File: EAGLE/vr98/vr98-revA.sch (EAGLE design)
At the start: 454 parts, among them Q1 2N7002, Q2 DMG2305UX-7, Q3 IRLML6401, Q4 2N2222, U1 STM32F411CEU7, U2 74HC589A_DT, U3 74HC589A_DT, U4 74HC589A_DT, U5 M25C, Y1 32.768kHz ±20ppm 6pF, Y2 25MHz 9pF

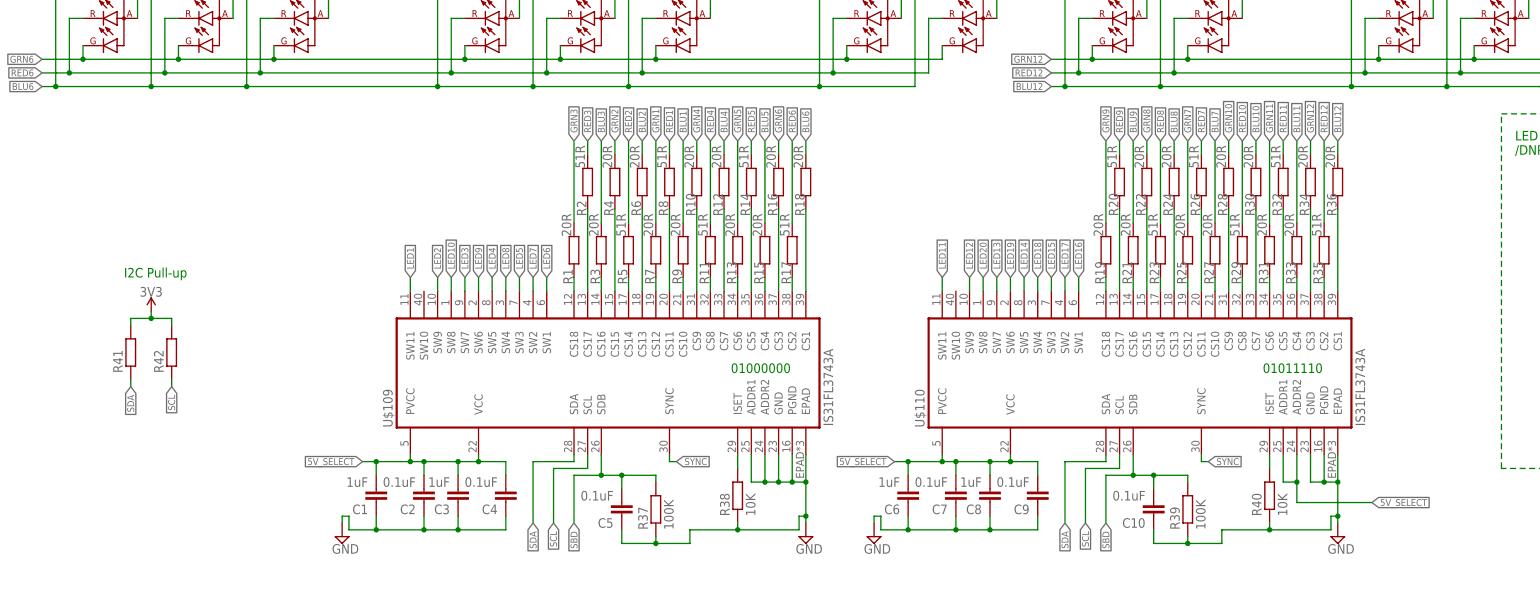
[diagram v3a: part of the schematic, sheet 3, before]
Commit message: move to ISP LED driver
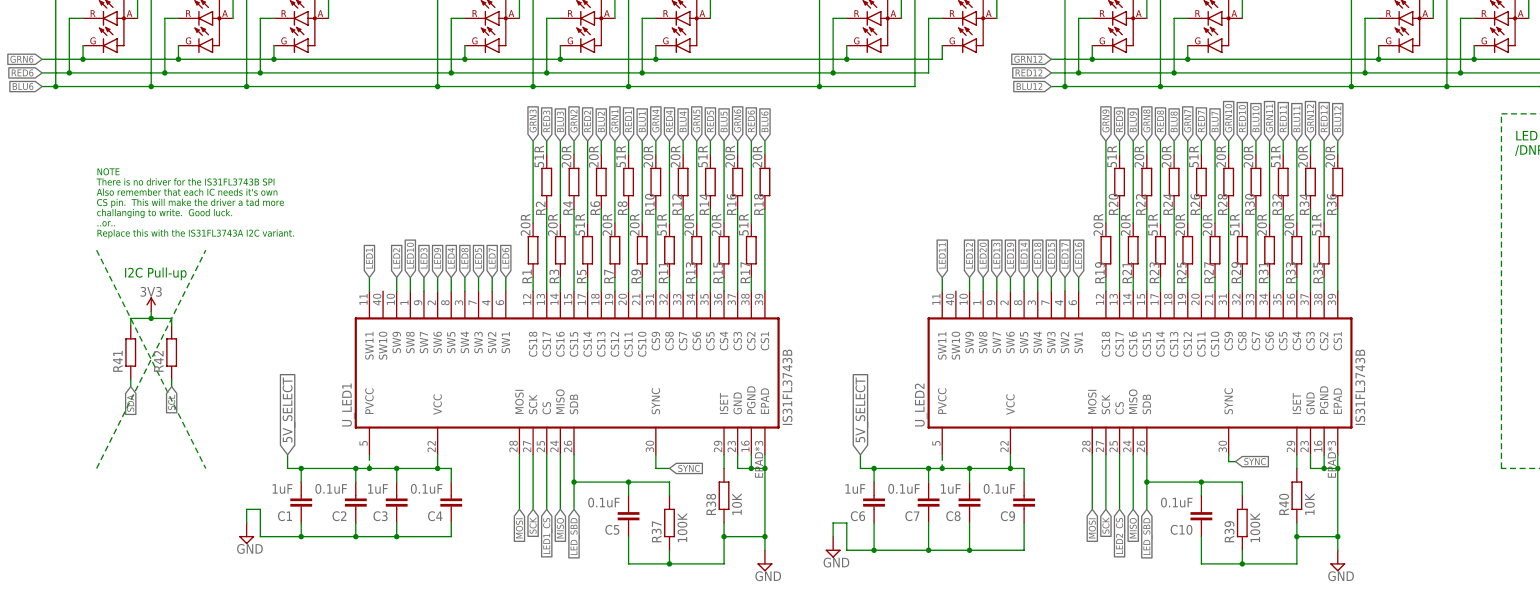
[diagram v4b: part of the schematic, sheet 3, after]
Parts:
- removed U$109, U$110: IS31FL3743A, __untitled:IS31FL3743A
- added U_LED1, U_LED2: IS31FL3743B, ts_kb_mcu:IS31FL3743B
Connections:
- removed net N$137: R40.2, U$110.ISET
- removed net RX: U1A.PA10
- removed net SBD: C10.2, C5.2, R37.2, R39.2, U$109.SDB, U$110.SDB
- removed net TX: U1A.PA9
- new net LED1_CS: U1A.PA9, U_LED1.CS
- new net LED2_CS: U1A.PA10, U_LED2.CS
- new net LED_SBD: C10.2, C5.2, R37.2, R39.2, U_LED1.SDB, U_LED2.SDB
- new net LED_SDB: U1A.PB5
- new net N$151: R40.2, U_LED2.ISET
- net 5V_SELECT: now also U_LED1.PVCC, U_LED1.VCC, U_LED2.PVCC, U_LED2.VCC; no longer U$109.PVCC, U$109.VCC, U$110.ADDR1, U$110.ADDR2, U$110.PVCC, U$110.VCC
- net GND: now also U_LED1.EPAD, U_LED1.GND, U_LED1.PGND, U_LED2.EPAD, U_LED2.GND, U_LED2.PGND; no longer U$109.ADDR1, U$109.ADDR2, U$109.EPAD, U$109.GND, U$109.PGND, U$110.EPAD, U$110.GND, U$110.PGND
- net LED1: now also U_LED1.SW11; no longer U$109.SW11
- net LED10: now also U_LED1.SW8; no longer U$109.SW8
- net LED11: now also U_LED2.SW11; no longer U$110.SW11
- net LED12: now also U_LED2.SW9; no longer U$110.SW9
- net LED13: now also U_LED2.SW7; no longer U$110.SW7
- net LED14: now also U_LED2.SW5; no longer U$110.SW5
- net LED15: now also U_LED2.SW3; no longer U$110.SW3
- net LED16: now also U_LED2.SW1; no longer U$110.SW1
- net LED17: now also U_LED2.SW2; no longer U$110.SW2
- net LED18: now also U_LED2.SW4; no longer U$110.SW4
- net LED19: now also U_LED2.SW6; no longer U$110.SW6
- net LED2: now also U_LED1.SW9; no longer U$109.SW9
- net LED20: now also U_LED2.SW8; no longer U$110.SW8
- net LED3: now also U_LED1.SW7; no longer U$109.SW7
- net LED4: now also U_LED1.SW5; no longer U$109.SW5
- net LED5: now also U_LED1.SW3; no longer U$109.SW3
- net LED6: now also U_LED1.SW1; no longer U$109.SW1
- net LED7: now also U_LED1.SW2; no longer U$109.SW2
- net LED8: now also U_LED1.SW4; no longer U$109.SW4
- net LED9: now also U_LED1.SW6; no longer U$109.SW6
- net MISO: now also U_LED1.MISO, U_LED2.MISO
- net MOSI: now also U_LED1.MOSI, U_LED2.MOSI
- net N$10: now also U_LED2.CS8; no longer U$110.CS8
- net N$11: now also U_LED2.CS9; no longer U$110.CS9
- net N$12: now also U_LED2.CS10; no longer U$110.CS10
- net N$123: now also U_LED1.CS5; no longer U$109.CS5
- net N$124: now also U_LED1.CS6; no longer U$109.CS6
- net N$125: now also U_LED1.CS7; no longer U$109.CS7
- net N$126: now also U_LED1.CS8; no longer U$109.CS8
- net N$127: now also U_LED1.CS9; no longer U$109.CS9
- net N$128: now also U_LED1.CS10; no longer U$109.CS10
- net N$129: now also U_LED1.CS11; no longer U$109.CS11
- net N$13: now also U_LED2.CS11; no longer U$110.CS11
- net N$130: now also U_LED1.CS12; no longer U$109.CS12
- net N$131: now also U_LED1.CS14; no longer U$109.CS14
- net N$132: now also U_LED1.CS15; no longer U$109.CS15
- net N$133: now also U_LED1.CS16; no longer U$109.CS16
- net N$134: now also U_LED1.CS17; no longer U$109.CS17
- net N$135: now also U_LED1.CS18; no longer U$109.CS18
- net N$136: now also U_LED1.ISET; no longer U$109.ISET
- net N$14: now also U_LED2.CS12; no longer U$110.CS12
- net N$15: now also U_LED2.CS14; no longer U$110.CS14
- net N$153: now also U_LED1.CS13; no longer U$109.CS13
- net N$16: now also U_LED2.CS15; no longer U$110.CS15
- net N$17: now also U_LED2.CS16; no longer U$110.CS16
- net N$18: now also U_LED2.CS17; no longer U$110.CS17
- net N$19: now also U_LED2.CS18; no longer U$110.CS18
- net N$20: now also U_LED2.CS13; no longer U$110.CS13
- net N$21: now also U_LED1.CS1; no longer U$109.CS1
- net N$22: now also U_LED1.CS2; no longer U$109.CS2
- net N$23: now also U_LED1.CS3; no longer U$109.CS3
- net N$24: now also U_LED1.CS4; no longer U$109.CS4
- net N$3: now also U_LED2.CS1; no longer U$110.CS1
- net N$4: now also U_LED2.CS2; no longer U$110.CS2
- net N$5: now also U_LED2.CS3; no longer U$110.CS3
- net N$6: now also U_LED2.CS4; no longer U$110.CS4
- net N$7: now also U_LED2.CS5; no longer U$110.CS5
- net N$8: now also U_LED2.CS6; no longer U$110.CS6
- net N$9: now also U_LED2.CS7; no longer U$110.CS7
- net SCK: now also U_LED1.SCK, U_LED2.SCK
- net SCL: no longer U$109.SCL, U$110.SCL
- net SDA: no longer U$109.SDA, U$110.SDA
- net SYNC: now also U_LED1.SYNC, U_LED2.SYNC; no longer U$109.SYNC, U$110.SYNC
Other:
- note added: "NOTE There is no driver for the IS31FL3743B SPI Also remember that each IC needs it's own CS pin. This will make the driver a tad more challanging to write. Good luck. ..or.. Replace this with the IS31FL3743A I2C variant."
- note removed: "01000000"
- note removed: "01011110"
- moved on the sheet: C1, C10, C2, C28, C3, C4, C5, C6, C7, C8, C9, R1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

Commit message: updates
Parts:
- removed D100, D103, D104: (no value), jlcpcb_basic_parts:1N5819WS
- removed J2: (no value), ts_keyboards:UBD-S1_C4
- removed R1, R10, R12, R13, R15, R16, R18, R19, R21, R22, R24, R25, R27, R28, R3, R30, R31, R33, R34, R36, R4, R6, R7, R9: 20R, rcl:R-EU_R0603
- removed R11, R14, R17, R2, R20, R23, R26, R29, R32, R35, R5, R8: 51R, rcl:R-EU_R0603
- removed R47, R48, R49, R50, R51, R52, R53, R54, R55, R56, R57, R58, R59, R60, R61, R62, R63, R64: 10K, rcl:R-EU_R0603
- removed S2: KEY, SparkFun-Switches:MOMENTARY-SWITCH-SPST-SMD-5.2-TALL-REDUNDANT
- removed SW_CL_2, SW_SPC_2, SW_SPC_3: MX-5-PIN-MILMAX-3305-XNO-SILK, ts_keyboards:MX-5-PIN-MILMAX-3305-XNO-SILK
- removed SW_DP_2, SW_ENT_2, SW_F13_2, SW_LS_2, SW_NUBS: MX-5-PIN-HOTSWAP-PADNO-SILK, ts_keyboards:MX-5-PIN-HOTSWAP-PADNO-SILK
- removed SW_FN: MX-5-PIN-HOTSWAP-PAD, ts_keyboards:MX-5-PIN-HOTSWAP-PAD
- removed U$100, U$32, U$38, U$58, U$75, U$83, U$99: 156120M173000, ts_keyboards:156120M173000
- removed U$108: DNP, ts_keyboards:156120M173000
- added H_BSP, H_ENT, H_LS, H_NEN, H_NP, H_RS: MX-STABS-200U, ts_keyboards:MX-STABS-200U
- added H_SPC: MX-STABS-625U, ts_keyboards:MX-STABS-625U
- added RA1, RA2, RA3, RA4, RA5: 10K, __untitled:R-EU-4_
- added RA10, RA13, RA14, RA15, RA8, RA9: 20R, __untitled:R-EU-4_
- added RA11, RA12, RA6, RA7: 51R, __untitled:R-EU-4_
- added UDB1: (no value), ts_keyboards:UBD-S1_C4
- added UDB2: (no value), ts_keyboards:UBD-C3
- added Z1, Z10, Z101, Z103, Z104, Z107, Z11, Z12, Z13, Z14, Z15, Z16, Z17, Z2, Z20, Z21, Z22, Z23, Z24, Z25, Z26, Z27, Z28, Z3, Z4, Z6, Z7, Z8, Z9, Z94: 156120M173000, ts_keyboards:156120M173000
- added Z19: DNP, ts_keyboards:156120M173000
- D101: value (none) -> DNP
- J1: device ts_keyboards:UBD-C3 -> SparkFun-Connectors:CONN_02
- JKEY: value (none) -> MOLEX_0781710005; device __untitled:MOLEX_0781710004 -> molex-pico-ezmate:MOLEX_0781710005
- SW_F17: device untitled:EC11E15244B2 -> ts_keyboards:EC11E15244B2
- U$1, U$10, U$11, U$12, U$13, U$14, U$15, U$16, U$17, U$18, U$19, U$2, U$20, U$21, U$22, U$23, U$24, U$25, U$26, U$27, U$6, U$7, U$8, U$9: value 156120M173000 -> TEST_PAD; device ts_keyboards:156120M173000 -> ts_keyboards:TEST_PAD
- U$3, U$4: value 156120M173000 -> MOLEX_0781710006; device ts_keyboards:156120M173000 -> molex-pico-ezmate:MOLEX_0781710006
- renumbered U$101 to Z92, U$102 to Z93, U$103 to Z95, U$104 to Z96, U$105 to Z97, U$106 to Z98, U$107 to Z99, U$28 to Z29, U$29 to Z30, U$30 to Z31, U$31 to Z32, U$33 to Z33, U$34 to Z34, U$35 to Z35, U$36 to Z36, U$37 to Z37, U$39 to Z38, U$40 to Z39, U$41 to Z40, U$42 to Z41, U$43 to Z42, U$44 to Z43, U$45 to Z44, U$46 to Z45, U$47 to Z46, U$48 to Z47, U$49 to Z48, U$5 to Z5, U$50 to Z49, U$51 to Z50, U$52 to Z102, U$53 to Z51, U$54 to Z52, U$55 to Z53, U$56 to Z54, U$57 to Z55, U$59 to Z56, U$60 to Z57, U$61 to Z58, U$62 to Z59, U$63 to Z60, U$64 to Z61, U$65 to Z62, U$66 to Z63, U$67 to Z64, U$68 to Z65, U$69 to Z66, U$70 to Z67, U$71 to Z68, U$72 to Z69, U$73 to Z70, U$74 to Z71, U$76 to Z72, U$77 to Z73, U$78 to Z74, U$79 to Z75, U$80 to Z76, U$81 to Z77, U$82 to Z78, U$84 to Z79, U$85 to Z80, U$86 to Z81, U$87 to Z82, U$88 to Z83, U$89 to Z84, U$90 to Z85, U$91 to Z86, U$92 to Z87, U$93 to Z88, U$94 to Z89, U$95 to Z90, U$96 to Z105, U$97 to Z91, U$98 to Z106
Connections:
- net LED_EN renamed LED_PWR_EN
- removed net K_F13: D18.A, SW_F13_2.S, SW_F17.D
- new net N$152: SW_F17.A, U$4.5
- new net N$156: D102.A, JKEY.5
- new net N$157: D18.A, U$3.4
- net BLU1: now also RA9B.1, Z1.B, Z2.B, Z3.B, Z4.B, Z6.B, Z7.B, Z8.B, Z9.B; no longer R9.2, U$1.B, U$2.B, U$3.B, U$4.B, U$6.B, U$7.B, U$8.B, U$9.B
- net BLU10: now also RA14D.2, Z103.B; no longer R30.2
- net BLU11: now also RA15B.1; no longer R33.2
- net BLU12: now also RA15D.2, Z94.B; no longer R36.2
- net BLU2: now also RA8D.2, Z19.B, Z20.B, Z21.B, Z22.B, Z23.B, Z24.B, Z25.B, Z26.B, Z27.B, Z28.B; no longer R6.2, U$18.B, U$19.B, U$20.B, U$21.B, U$22.B, U$23.B, U$24.B, U$25.B, U$26.B, U$27.B
- net BLU3: now also RA8B.1; no longer R3.2, U$38.B
- net BLU4: now also RA9D.2; no longer R12.2, U$58.B
- net BLU5: now also RA10B.1; no longer R15.2, U$75.B, U$83.B
- net BLU6: now also RA10D.2, Z104.B, Z107.B; no longer R18.2, U$100.B, U$99.B
- net BLU7: now also RA14B.1, Z10.B, Z11.B, Z12.B, Z13.B, Z14.B, Z15.B, Z16.B, Z17.B; no longer R27.2, U$10.B, U$108.B, U$11.B, U$12.B, U$13.B, U$14.B, U$15.B, U$16.B, U$17.B
- net BLU8: now also RA13D.2, Z101.B; no longer R24.2, U$32.B
- net BLU9: now also RA13B.1; no longer R21.2
- net COL0: now also RA1A.2, U$11.P$1; no longer R47.2
- net COL1: now also RA1B.1, U$12.P$1; no longer R48.2
- net COL10: now also D94.C, RA3C.1, U$21.P$1; no longer D95.C, R57.2
- net COL11: now also RA3D.2, U$22.P$1; no longer R58.2
- net COL12: now also D95.C, RA4A.2, U$23.P$1; no longer D96.C, R59.2
- net COL13: now also D96.C, RA4B.1, U$24.P$1; no longer D97.C, R60.2, SW_DP_2.P, SW_ENT_2.P
- net COL14: now also D97.C, RA4C.1, U$25.P$1; no longer D98.C, R61.2
- net COL15: now also D98.C, RA4D.2, U$26.P$1; no longer D99.C, R62.2
- net COL16: now also D99.C, RA5A.2, U$27.P$1; no longer D100.C, R63.2
- net COL17: now also RA5B.1, U$1.P$1; no longer R64.2, SW_F13_2.P
- net COL2: now also RA1C.1, U$13.P$1; no longer D101.C, R49.2
- net COL3: now also RA1D.2, U$14.P$1; no longer D103.C, R50.2
- net COL4: now also D101.C, RA2A.2, U$15.P$1; no longer D102.C, R51.2
- net COL5: now also RA2B.1, U$16.P$1; no longer R52.2
- net COL6: now also D102.C, RA2C.1, U$17.P$1; no longer D104.C, R53.2
- net COL7: now also RA2D.2, U$18.P$1; no longer D92.C, R54.2
- net COL8: now also D92.C, RA3A.2, U$19.P$1; no longer D93.C, R55.2
- net COL9: now also D93.C, RA3B.1, U$20.P$1; no longer D94.C, R56.2
- net ENC_A: now also R43.1, U$3.6; no longer R44.1, SW_F17.A
- net ENC_B: now also R44.1, U$3.5; no longer R43.1, SW_F17.B
- net GND: now also J1.1, JKEY.1, JKEY.M, SW_F17.GND, U$3.1, U$3.M, U$4.1, U$4.M, UDB1.GND, UDB1.M, UDB2.GND, UDB2.M; no longer J1.GND, J2.GND, JKEY.4, SW_F17.1, SW_F17.2, SW_F17.C
- net GND2: now also RA1A.1, RA1B.2, RA1C.2, RA1D.1, RA2A.1, RA2B.2, RA2C.2, RA2D.1, RA3A.1, RA3B.2, RA3C.2, RA3D.1, RA4A.1, RA4B.2, RA4C.2, RA4D.1, RA5A.1, RA5B.2; no longer R47.1, R48.1, R49.1, R50.1, R51.1, R52.1, R53.1, R54.1, R55.1, R56.1, R57.1, R58.1, R59.1, R60.1, R61.1, R62.1, R63.1, R64.1
- net GRN1: now also RA9A.2, Z1.G, Z2.G, Z3.G, Z4.G, Z6.G, Z7.G, Z8.G, Z9.G; no longer R7.2, U$1.G, U$2.G, U$3.G, U$4.G, U$6.G, U$7.G, U$8.G, U$9.G
- net GRN10: now also RA14C.1, Z103.G; no longer R28.2
- net GRN11: now also RA15A.2; no longer R31.2
- net GRN12: now also RA15C.1, Z94.G; no longer R34.2
- net GRN2: now also RA8C.1, Z19.G, Z20.G, Z21.G, Z22.G, Z23.G, Z24.G, Z25.G, Z26.G, Z27.G, Z28.G; no longer R4.2, U$18.G, U$19.G, U$20.G, U$21.G, U$22.G, U$23.G, U$24.G, U$25.G, U$26.G, U$27.G
- net GRN3: now also RA8A.2; no longer R1.2, U$38.G
- net GRN4: now also RA9C.1; no longer R10.2, U$58.G
- net GRN5: now also RA10A.2; no longer R13.2, U$75.G, U$83.G
- net GRN6: now also RA10C.1, Z104.G, Z107.G; no longer R16.2, U$100.G, U$99.G
- net GRN7: now also RA14A.2, Z10.G, Z11.G, Z12.G, Z13.G, Z14.G, Z15.G, Z16.G, Z17.G; no longer R25.2, U$10.G, U$108.G, U$11.G, U$12.G, U$13.G, U$14.G, U$15.G, U$16.G, U$17.G
- net GRN8: now also RA13C.1, Z101.G; no longer R22.2, U$32.G
- net GRN9: now also RA13A.2; no longer R19.2
- net K_CL: no longer SW_CL_2.P
- net K_DP: no longer SW_DP_2.S
- net K_ENT: no longer SW_ENT_2.S
- net K_LS: no longer SW_LS_2.P
- net LED1: now also Z1.A, Z19.A; no longer U$1.A, U$18.A
- net LED10: now also Z28.A, Z9.A; no longer U$100.A, U$27.A, U$83.A, U$9.A
- net LED11: now also Z10.A; no longer U$10.A
- net LED12: now also Z11.A; no longer U$11.A
- net LED13: now also Z12.A, Z94.A; no longer U$12.A
- net LED14: now also Z13.A; no longer U$13.A
- net LED15: no longer U$32.A
- net LED16: now also Z101.A, Z103.A, Z14.A; no longer U$14.A
- net LED17: now also Z15.A; no longer U$15.A
- net LED18: now also Z16.A; no longer U$16.A
- net LED19: now also Z17.A; no longer U$17.A
- net LED2: now also Z20.A; no longer U$19.A, U$38.A, U$58.A, U$75.A
- net LED20: no longer U$108.A
- net LED3: now also Z2.A, Z21.A; no longer U$2.A, U$20.A
- net LED4: now also Z104.A, Z22.A, Z3.A; no longer U$21.A, U$3.A
- net LED5: now also Z23.A, Z4.A; no longer U$22.A, U$4.A
- net LED6: now also Z24.A; no longer U$23.A
- net LED7: now also Z25.A, Z6.A; no longer U$24.A, U$6.A
- net LED8: now also Z107.A, Z26.A, Z7.A; no longer U$25.A, U$7.A
- net LED9: now also Z27.A, Z8.A; no longer U$26.A, U$8.A, U$99.A
- net N$10: now also RA12D.1; no longer R29.1
- net N$102: now also D98.A; no longer D99.A
- net N$103: now also D97.A; no longer D98.A
- net N$104: now also D96.A; no longer D97.A
- net N$105: now also D95.A; no longer D96.A
- net N$106: now also SW_F17.E, U$4.3; no longer D95.A, SW_FN.P
- net N$11: now also RA14C.2; no longer R28.1
- net N$114: now also D99.A; no longer D100.A
- net N$12: now also RA14B.2; no longer R27.1
- net N$123: now also RA7A.1; no longer R14.1
- net N$124: now also RA10A.1; no longer R13.1
- net N$125: now also RA9D.1; no longer R12.1
- net N$126: now also RA6D.1; no longer R11.1
- net N$127: now also RA9C.2; no longer R10.1
- net N$128: now also RA9B.2; no longer R9.1
- net N$129: now also RA6C.2; no longer R8.1
- net N$13: now also RA12C.2; no longer R26.1
- net N$130: now also RA9A.1; no longer R7.1
- net N$131: now also RA6B.2; no longer R5.1
- net N$132: now also RA8C.2; no longer R4.1
- net N$133: now also RA8B.2; no longer R3.1
- net N$134: now also RA6A.1; no longer R2.1
- net N$135: now also RA8A.1; no longer R1.1
- net N$14: now also RA14A.1; no longer R25.1
- net N$142: now also SW_F17.D, U$4.4; no longer D101.A, SW_NUBS.P
- net N$144: now also D101.A; no longer D102.A, S2.1
- net N$146: now also J1.2
- net N$15: now also RA12B.2; no longer R23.1
- net N$153: now also RA8D.1; no longer R6.1
- net N$154: now also SW_F17.B, U$4.6; no longer D103.A, SW_SPC_2.P
- net N$155: now also SW_F17.C; no longer D104.A, SW_SPC_3.P
- net N$16: now also RA13C.2; no longer R22.1
- net N$17: now also RA13B.2; no longer R21.1
- net N$18: now also RA12A.1; no longer R20.1
- net N$19: now also RA13A.1; no longer R19.1
- net N$20: now also RA13D.1; no longer R24.1
- net N$21: now also RA10D.1; no longer R18.1
- net N$22: now also RA7B.2; no longer R17.1
- net N$23: now also RA10C.2; no longer R16.1
- net N$24: now also RA10B.2; no longer R15.1
- net N$3: now also RA15D.1; no longer R36.1
- net N$4: now also RA11B.2; no longer R35.1
- net N$5: now also RA15C.2; no longer R34.1
- net N$6: now also RA15B.2; no longer R33.1
- net N$7: now also RA11A.1; no longer R32.1
- net N$8: now also RA15A.1; no longer R31.1
- net N$9: now also RA14D.1; no longer R30.1
- net RED1: now also RA6C.1, Z1.R, Z2.R, Z3.R, Z4.R, Z6.R, Z7.R, Z8.R, Z9.R; no longer R8.2, U$1.R, U$2.R, U$3.R, U$4.R, U$6.R, U$7.R, U$8.R, U$9.R
- net RED10: now also RA12D.2, Z103.R; no longer R29.2
- net RED11: now also RA11A.2; no longer R32.2
- net RED12: now also RA11B.1, Z94.R; no longer R35.2
- net RED2: now also RA6B.1, Z19.R, Z20.R, Z21.R, Z22.R, Z23.R, Z24.R, Z25.R, Z26.R, Z27.R, Z28.R; no longer R5.2, U$18.R, U$19.R, U$20.R, U$21.R, U$22.R, U$23.R, U$24.R, U$25.R, U$26.R, U$27.R
- net RED3: now also RA6A.2; no longer R2.2, U$38.R
- net RED4: now also RA6D.2; no longer R11.2, U$58.R
- net RED5: now also RA7A.2; no longer R14.2, U$75.R, U$83.R
- net RED6: now also RA7B.1, Z104.R, Z107.R; no longer R17.2, U$100.R, U$99.R
- net RED7: now also RA12C.1, Z10.R, Z11.R, Z12.R, Z13.R, Z14.R, Z15.R, Z16.R, Z17.R; no longer R26.2, U$10.R, U$108.R, U$11.R, U$12.R, U$13.R, U$14.R, U$15.R, U$16.R, U$17.R
- net RED8: now also RA12B.1, Z101.R; no longer R23.2, U$32.R
- net RED9: now also RA12A.2; no longer R20.2
- net ROW0: now also U$2.P$1, U$3.3; no longer SW_F17.E
- net ROW1: now also U$6.P$1
- net ROW2: now also U$7.P$1
- net ROW3: now also U$8.P$1; no longer SW_CL_2.S
- net ROW4: now also U$9.P$1; no longer SW_LS_2.S, SW_NUBS.S
- net ROW5: now also JKEY.4, U$10.P$1; no longer S2.2, SW_FN.S, SW_SPC_2.S, SW_SPC_3.S
- net USB_DN: now also UDB1.DN, UDB2.DN; no longer J1.D-, J2.D-
- net USB_DP: now also UDB1.DP, UDB2.DP; no longer J1.D+, J2.D+
- net VCC_1: now also UDB1.VCC, UDB2.VCC; no longer J1.VCC, J2.VCC
- net VCC_2: now also U$3.2; no longer JKEY.1
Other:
- note added: "(Optional) DIP_SWITCH_1"
- note added: "DNP Unified Daughter Board (C3) Conn. (Legacy)"
- note removed: "(SW_NEN_2)"
- note removed: "(SW_NP_2)"
- note removed: "DIP_SWITCH"
- note removed: "DNP Unified Daughter Board (C3) Conn."
- note removed: "ISO KEY SET"
- note removed: "JIS VARIENT (SW_BSP_2)"
- note removed: "JIS VARIENT (SW_RS_2)"
- note removed: "JIS VARIENT SW_SPC_2"
- note removed: "JIS VARIENT SW_SPC_3"
- note removed: "SPLIT SPACE"
- note removed: "STEP CAPS-LOCK"
- note removed: "SW_NUBS"

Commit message: wip
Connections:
- net COL10: now also U3.E; no longer U3.F
- net COL11: now also D95.C, U3.F; no longer U3.G
- net COL12: now also D96.C, U3.G; no longer D95.C, U4.B
- net COL13: now also D97.C, U3.H; no longer D96.C, U4.C
- net COL14: now also U4.B; no longer D97.C, U4.D
- net COL15: now also U4.C; no longer U4.E
- net COL16: now also U4.D; no longer U4.F
- net COL17: now also U4.E; no longer U4.G
- net COL6: now also U2.H; no longer U3.B
- net COL7: now also U3.B; no longer U3.C
- net COL8: now also U3.C; no longer U3.D
- net COL9: now also U3.D; no longer U3.E
- net GND: now also U4.F, U4.G; no longer U2.H, U3.H
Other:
- moved on the sheet: D15, D16, D17, D18, D33, D34, D35, D36, D51, D52, D53, D54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

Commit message: wip
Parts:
- removed U$1, U$10, U$11, U$12, U$13, U$14, U$15, U$16, U$17, U$18, U$19, U$2, U$20, U$21, U$22, U$23, U$24, U$25, U$26, U$27, U$6, U$7, U$8, U$9: TEST_PAD, ts_keyboards:TEST_PAD
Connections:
- net COL0: no longer U$11.P$1
- net COL1: no longer U$12.P$1
- net COL10: no longer U$21.P$1
- net COL11: no longer U$22.P$1
- net COL12: no longer U$23.P$1
- net COL13: no longer U$24.P$1
- net COL14: no longer U$25.P$1
- net COL15: no longer U$26.P$1
- net COL16: no longer U$27.P$1
- net COL17: no longer U$1.P$1
- net COL2: no longer U$13.P$1
- net COL3: no longer U$14.P$1
- net COL4: no longer U$15.P$1
- net COL5: no longer U$16.P$1
- net COL6: no longer U$17.P$1
- net COL7: no longer U$18.P$1
- net COL8: no longer U$19.P$1
- net COL9: no longer U$20.P$1
- net ROW0: no longer U$2.P$1
- net ROW1: no longer U$6.P$1
- net ROW2: no longer U$7.P$1
- net ROW3: no longer U$8.P$1
- net ROW4: no longer U$9.P$1
- net ROW5: no longer U$10.P$1

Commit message: wip
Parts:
- removed C31: 100nF, rcl:C-EUC0603
- removed Q3: IRLML6401, SparkFun-DiscreteSemi:MOSFET_PCH-IRLML2244
- removed Q4: 2N2222, SparkFun-DiscreteSemi:TRANS_NPN-MMBT2222AL
- removed R72: 1K, rcl:R-EU_R0603
- removed R73: 100K, rcl:R-EU_R0603
- added U6: TPS22995H-Q1, __untitled:TPS22995H-Q1
- R71: value 100K -> 1K
- U1: value STM32F411CEU7 -> STM32F411CEU7THERM; device st:STM32F411CEU7 -> st:STM32F411CEU7THERM
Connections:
- net 5V_SELECT renamed VCC_LED
- net N$122 renamed Y1O
- net N$138 renamed Y2I
- net N$139 renamed Y2O
- net N$143 renamed VREF+
- net N$146 renamed RESET
- net N$79 renamed Y1I
- removed net LED_VCC: C31.1, J_5V.1, Q3.D
- removed net N$147: Q4.C, R72.1
- removed net N$148: C31.2, Q3.G, R71.1, R72.2
- removed net N$153: RA8D.1, U_LED1.CS13
- removed net N$70: Q4.B, R73.1
- removed net UDB_DP: R46.1
- new net LOAD_SWITCH_OUT: J_5V.1, U6.OUT
- new net N$122: RA8B.1, U_LED1.CS15
- new net N$79: RA8A.1, U_LED1.CS13
- net BLU1: now also RA9C.2; no longer RA9B.1
- net BLU2: now also RA8A.2; no longer RA8D.2
- net BLU3: now also RA8C.2; no longer RA8B.1
- net BLU4: now also RA9A.2; no longer RA9D.2
- net COL0: now also RA4A.2; no longer RA1A.2
- net COL1: now also RA4B.2; no longer RA1B.1
- net COL10: now also RA2D.2; no longer RA3C.1
- net COL11: now also RA3A.2; no longer RA3D.2
- net COL12: now also RA3B.2; no longer RA4A.2
- net COL13: now also RA3C.2; no longer RA4B.1
- net COL14: now also RA1A.2; no longer RA4C.1
- net COL15: now also RA1B.2; no longer RA4D.2
- net COL16: now also RA1C.2; no longer RA5A.2
- net COL17: now also RA1D.2; no longer RA5B.1
- net COL2: now also RA4C.2; no longer RA1C.1
- net COL3: now also RA4D.2; no longer RA1D.2
- net COL4: now also RA5A.2; no longer RA2A.2
- net COL5: now also RA5B.2; no longer RA2B.1
- net COL6: now also RA5C.2; no longer RA2C.1
- net COL7: now also RA2A.2; no longer RA2D.2
- net COL8: now also RA2B.2; no longer RA3A.2
- net COL9: now also RA2C.2; no longer RA3B.1
- net GND: now also R71.1, U6.G; no longer Q4.E
- net GND2: now also RA1B.1, RA1C.1, RA2B.1, RA2C.1, RA3B.1, RA3C.1, RA4B.1, RA4C.1, RA5B.1, RA5C.1, RA5D.1; no longer RA1B.2, RA1C.2, RA2B.2, RA2C.2, RA3B.2, RA3C.2, RA4B.2, RA4C.2, RA5B.2
- net GRN1: now also RA9D.2; no longer RA9A.2
- net GRN2: now also RA8B.2; no longer RA8C.1
- net GRN3: now also RA8D.2; no longer RA8A.2
- net GRN4: now also RA9B.2; no longer RA9C.1
- net LED_PWR_EN: now also U6.ON; no longer R73.2
- net N$123: now also RA7B.1; no longer RA7A.1
- net N$125: now also RA9C.1, U_LED1.CS10; no longer RA9D.1, U_LED1.CS7
- net N$126: now also RA6B.1, U_LED1.CS11; no longer RA6D.1, U_LED1.CS8
- net N$127: now also RA9B.1; no longer RA9C.2
- net N$128: now also RA7D.1, U_LED1.CS8; no longer RA9B.2, U_LED1.CS10
- net N$129: now also RA6C.1, U_LED1.CS14; no longer RA6C.2, U_LED1.CS11
- net N$130: now also U_LED1.CS7; no longer U_LED1.CS12
- net N$131: now also RA6D.1, U_LED1.CS17; no longer RA6B.2, U_LED1.CS14
- net N$132: now also RA7C.1, U_LED1.CS2; no longer RA8C.2, U_LED1.CS15
- net N$133: now also RA8C.1; no longer RA8B.2
- net N$134: now also RA8D.1, U_LED1.CS18; no longer RA6A.1, U_LED1.CS17
- net N$135: now also R71.2, U6.RT; no longer RA8A.1, U_LED1.CS18
- net N$22: now also RA9D.1, U_LED1.CS12; no longer RA7B.2, U_LED1.CS2
- net RED1: now also RA6B.2; no longer RA6C.1
- net RED2: now also RA6C.2; no longer RA6B.1
- net RED3: now also RA6D.2; no longer RA6A.2
- net RED4: now also RA7D.2; no longer RA6D.2
- net RED5: now also RA7B.2; no longer RA7A.2
- net RED6: now also RA7C.2; no longer RA7B.1
- net USB_DP: now also R46.1
- net VCC_1: now also U6.BI, U6.IN; no longer Q3.S, R71.2
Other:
- moved on the sheet: J_5V, R71, RA1B, RA1C, RA2B, RA2C, RA3B, RA3C, RA4B, RA4C, RA5B, RA5C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
